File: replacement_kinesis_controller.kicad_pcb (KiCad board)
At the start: 2 copper layers, 99.1 x 86.4 mm, 78 parts, among them CN1 USB_general, CN4 USB_general, K1 CONN_3, K2 CONN_3, K3 CONN_3, K4 CONN_3, P1 CONN_3X2, P15 CONN_5X2, P16 CONN_16, P17 CONN_16, P18 POWER, P19 PCM, P2 CONN_13, P20 UART, P21 SPI, P22 IO, P23 SMIRF, P3 CONN_13, P4 CONN_10, P5 CONN_10, P6 CONN_13, P7 CONN_13, P8 CONN_5X2, P9 CONN_6, SW3 SPST, SW4 SPST, U1 MCP23018-E, U2 WS2811_RGB_LED, U3 WS2811_RGB_LED, U4 WS2811_RGB_LED, U5 WS2811_RGB_LED, U9 MCP1700

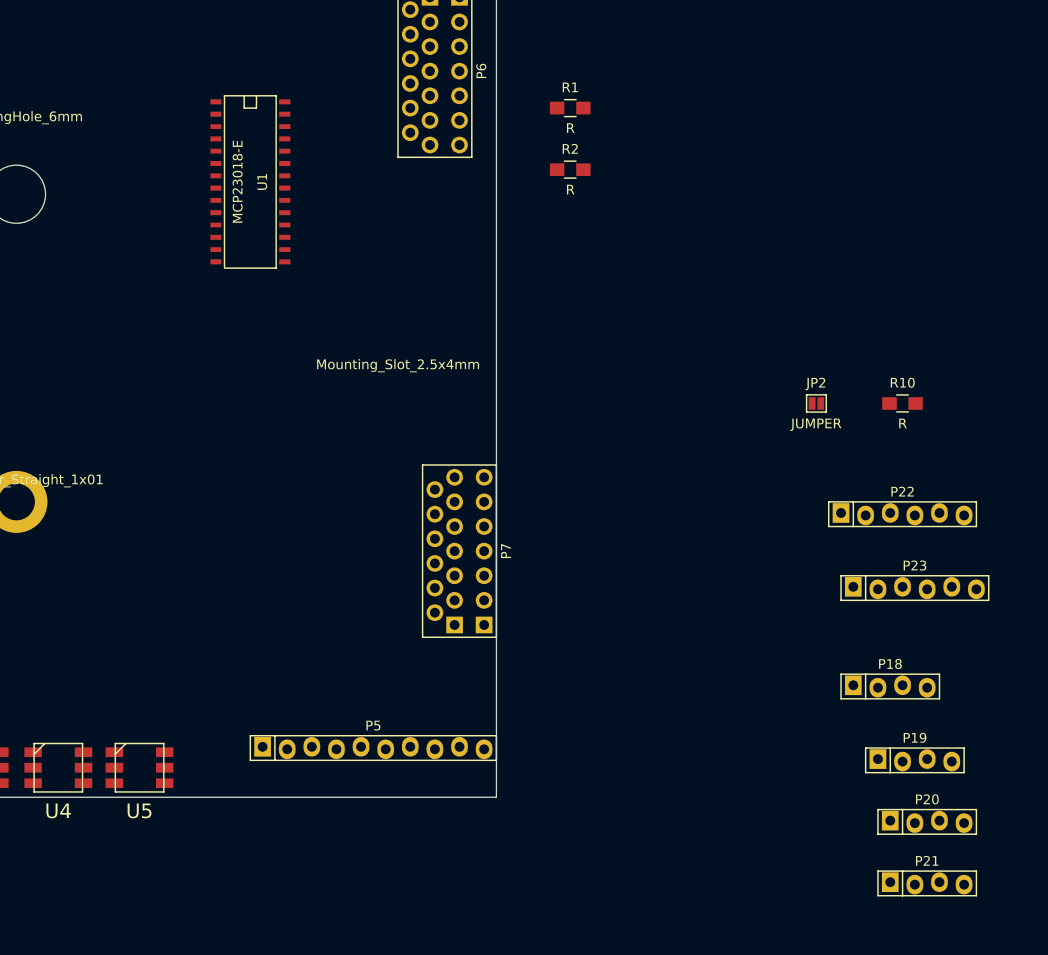
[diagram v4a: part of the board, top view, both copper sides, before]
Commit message: WT12 breakout headers are now in place
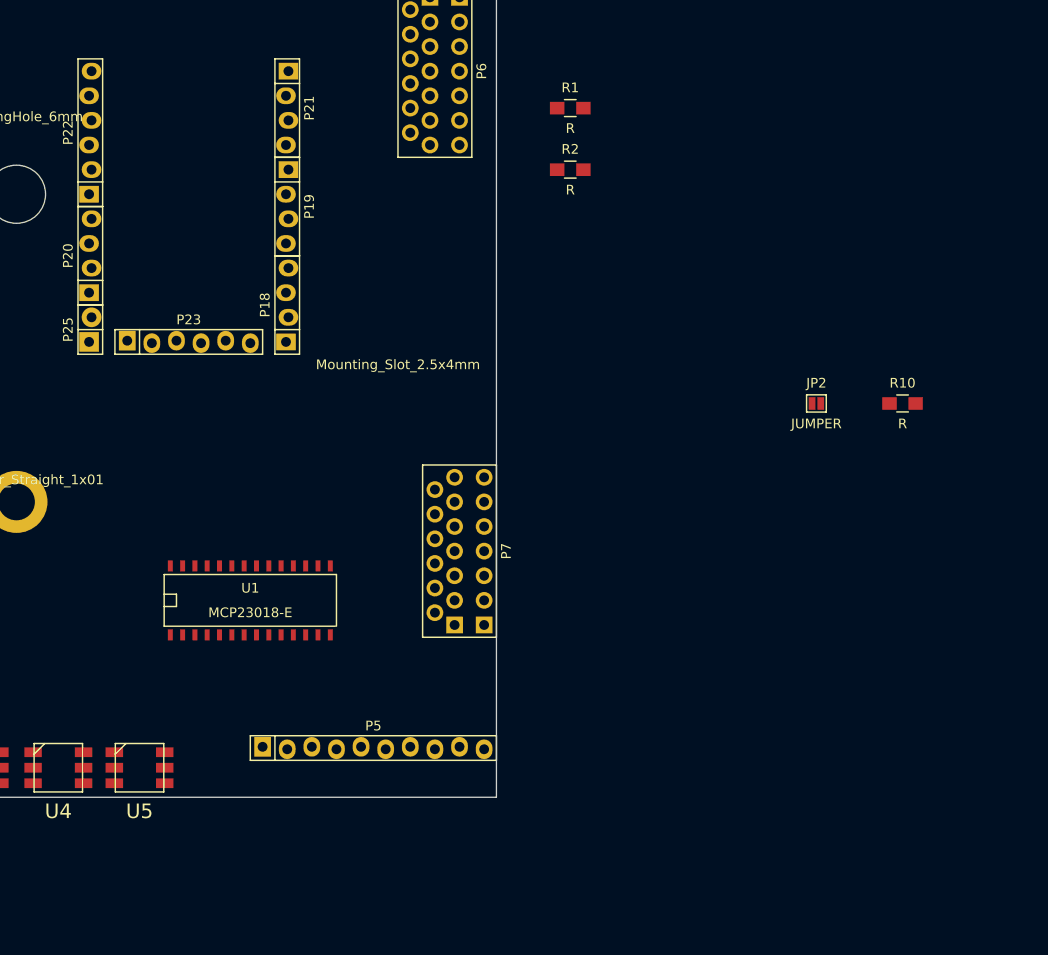
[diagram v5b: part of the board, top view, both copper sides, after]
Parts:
- added P25: USB, replacement_kinesis_controller:Pin_Header_Staggered_Straight_1x02, F.Cu at (130.8, 81.3)
- moved P20 104.3 mm to (130.8, 73.7), turned to 90 degrees
- moved P21 103.7 mm to (151.1, 58.4), turned to 270 degrees
- moved P22 92.6 mm to (130.8, 61.0), turned to 90 degrees
- moved P19 86.4 mm to (151.1, 68.6), turned to 270 degrees
- moved P23 79.1 mm to (141.0, 82.5)
- moved P18 73.6 mm to (151.1, 78.7), turned to 90 degrees
- moved U1 43.2 mm to (147.3, 109.2), turned to 0 degrees
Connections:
- net COL_0 renamed PF0
- net COL_1 renamed PF1
- net COL_11 renamed GPB5
- net COL_2 renamed PF4
- net COL_6 renamed GPB0
- net COL_8 renamed GPB2
- net GPA1 renamed ROW_R1
- net GPA3 renamed ROW_R3
- net GPB1 renamed COL_7
- net PB0 renamed ROW_L0
- net PB4 renamed ROW_L4
- net PB5 renamed ROW_L5
- net PD3 renamed W_RXD
- net PD6 renamed BAT_GUAGE
- net ROW_L2 renamed PB2
- net ROW_R4 renamed GPA4
- net ROW_R5 renamed GPA5
- net SDA renamed PD1

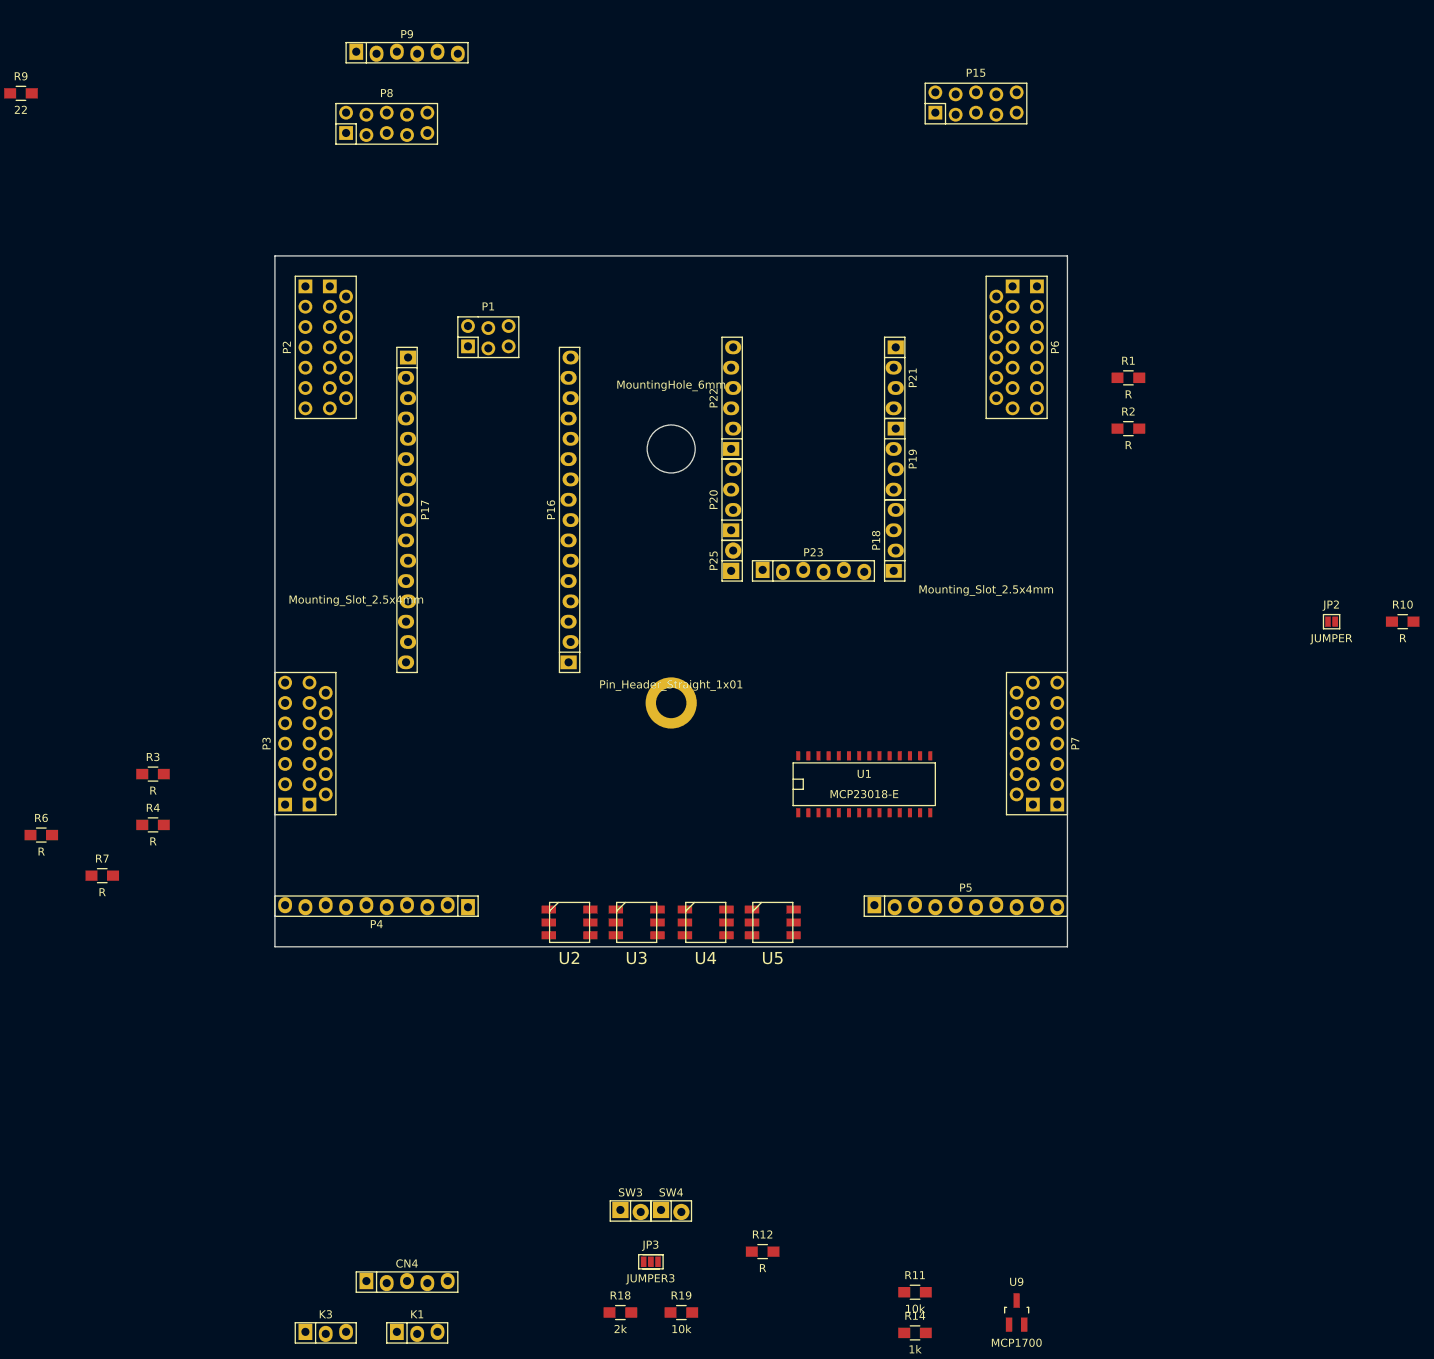
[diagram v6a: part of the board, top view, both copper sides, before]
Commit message: Move footprints around
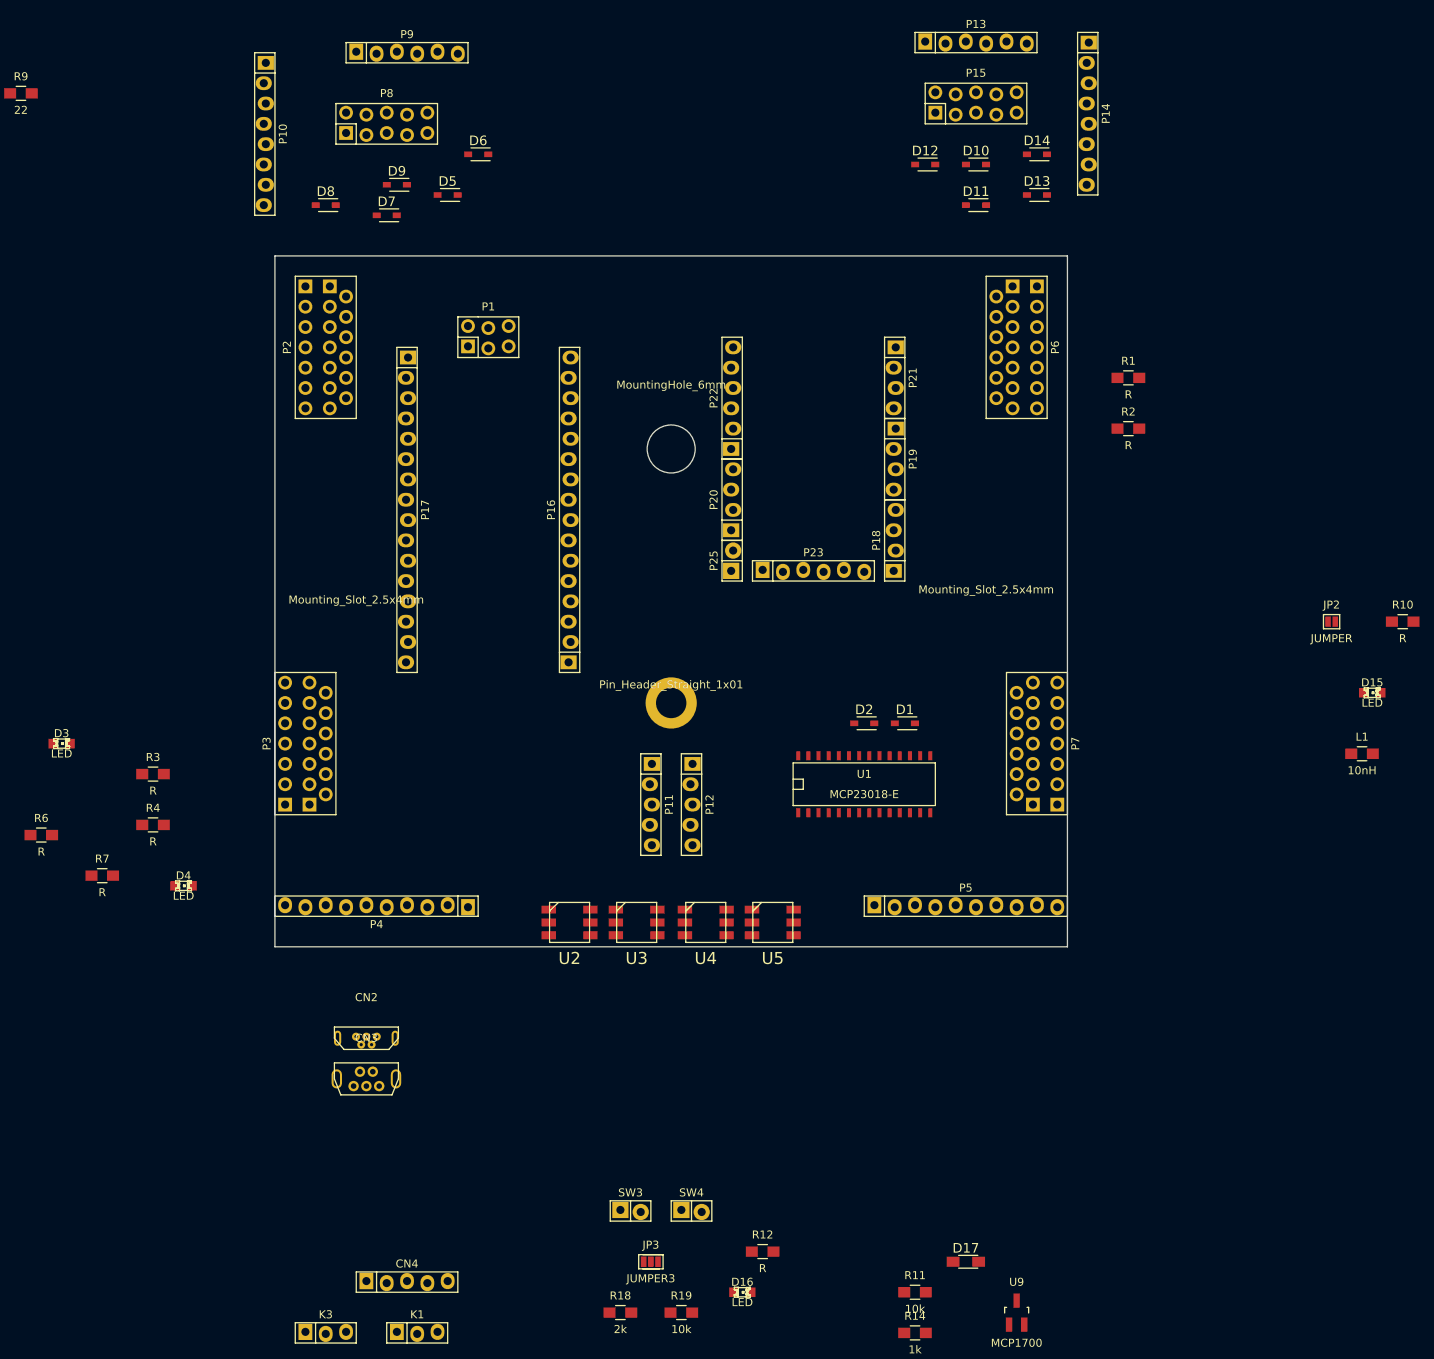
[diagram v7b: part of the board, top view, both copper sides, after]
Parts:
- added CN2: Micro-USB, replacement_kinesis_controller:USB_micro_B-vertical, F.Cu at (85.1, 141.0)
- added CN3: Mini-USB, replacement_kinesis_controller:USB_mini_B-vertical, F.Cu at (85.1, 146.1)
- added D1: DIODE, replacement_kinesis_controller:SOD-323_Handsolder, F.Cu at (152.4, 101.6)
- added D10: DIODE, replacement_kinesis_controller:SOD-323_Handsolder, F.Cu at (161.3, 31.8)
- added D11: DIODE, replacement_kinesis_controller:SOD-323_Handsolder, F.Cu at (161.3, 36.8)
- added D12: DIODE, replacement_kinesis_controller:SOD-323_Handsolder, F.Cu at (154.9, 31.8)
- added D13: DIODE, replacement_kinesis_controller:SOD-323_Handsolder, F.Cu at (168.9, 35.6)
- added D14: DIODE, replacement_kinesis_controller:SOD-323_Handsolder, F.Cu at (168.9, 30.5)
- added D15: LED, LEDs:LED-0805, F.Cu at (210.8, 97.8)
- added D16: LED, LEDs:LED-0805, F.Cu at (132.1, 172.7)
- added D17: DIODESCH, replacement_kinesis_controller:SOD-123_Handsolder, F.Cu at (160.0, 168.9)
- added D2: DIODE, replacement_kinesis_controller:SOD-323_Handsolder, F.Cu at (147.3, 101.6)
- added D3: LED, LEDs:LED-0805, F.Cu at (47.0, 104.1)
- added D4: LED, LEDs:LED-0805, F.Cu at (62.2, 121.9)
- added D5: DIODE, replacement_kinesis_controller:SOD-323_Handsolder, F.Cu at (95.2, 35.6)
- added D6: DIODE, replacement_kinesis_controller:SOD-323_Handsolder, F.Cu at (99.1, 30.5)
- added D7: DIODE, replacement_kinesis_controller:SOD-323_Handsolder, F.Cu at (87.6, 38.1)
- added D8: DIODE, replacement_kinesis_controller:SOD-323_Handsolder, F.Cu at (80.0, 36.8)
- added D9: DIODE, replacement_kinesis_controller:SOD-323_Handsolder, F.Cu at (88.9, 34.3)
- added L1: 10nH, Resistors_SMD:R_0805_HandSoldering, F.Cu at (209.6, 105.4)
- added P10: CONN_8, replacement_kinesis_controller:Pin_Header_Staggered_Straight_1x08, F.Cu at (72.4, 27.9)
- added P11: CONN_5, replacement_kinesis_controller:Pin_Header_Staggered_Straight_1x05, F.Cu at (120.7, 111.8)
- added P12: CONN_5, replacement_kinesis_controller:Pin_Header_Staggered_Straight_1x05, F.Cu at (125.7, 111.8)
- added P13: CONN_6, replacement_kinesis_controller:Pin_Header_Staggered_Straight_1x06, F.Cu at (161.3, 16.5)
- added P14: CONN_8, replacement_kinesis_controller:Pin_Header_Staggered_Straight_1x08, F.Cu at (175.3, 25.4)
- moved SW4 2.54 mm to (125.7, 162.6)
